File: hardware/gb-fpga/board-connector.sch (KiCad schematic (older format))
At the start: 1 part, among them J5 Conn_02x25_Counter_Clockwise

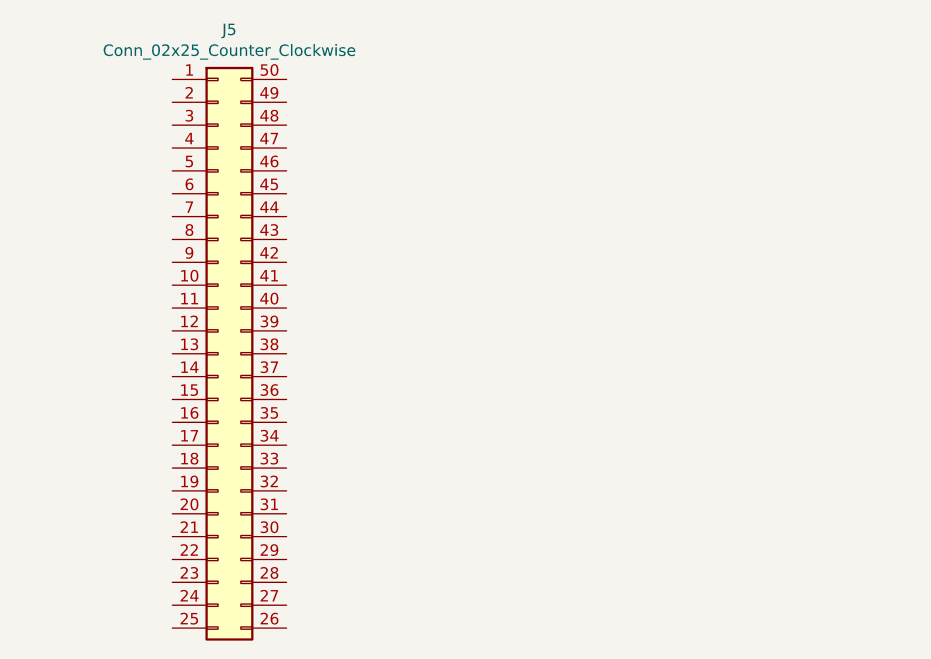
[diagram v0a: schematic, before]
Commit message: Add signals to board connector
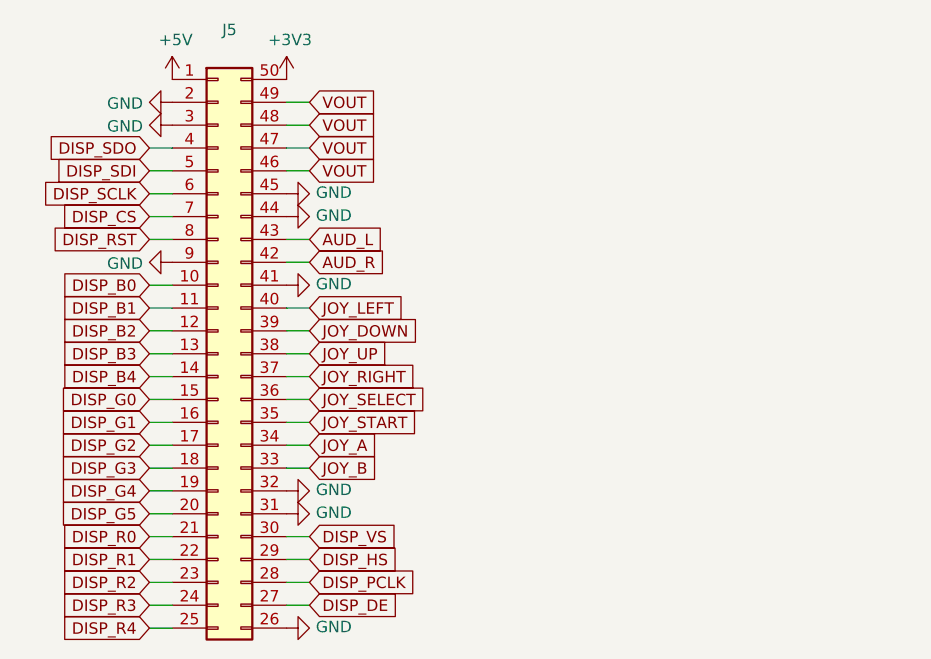
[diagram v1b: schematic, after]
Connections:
- net +5V: now reaches J5.1 (Pin_1)
- net DISP_B0: now reaches J5.10 (Pin_10)
- net DISP_B1: now reaches J5.11 (Pin_11)
- net DISP_B2: now reaches J5.12 (Pin_12)
- net DISP_B3: now reaches J5.13 (Pin_13)
- net DISP_B4: now reaches J5.14 (Pin_14)
- net DISP_G0: now reaches J5.15 (Pin_15)
- net DISP_G1: now reaches J5.16 (Pin_16)
- net DISP_G2: now reaches J5.17 (Pin_17)
- net DISP_G3: now reaches J5.18 (Pin_18)
- net DISP_G4: now reaches J5.19 (Pin_19)
- net GND: now reaches J5.2 (Pin_2)
- net GND: now also J5.26 (Pin_26), J5.3 (Pin_3), J5.31 (Pin_31), J5.32 (Pin_32), J5.41 (Pin_41), J5.44 (Pin_44), J5.45 (Pin_45), J5.9 (Pin_9)
- net DISP_G5: now reaches J5.20 (Pin_20)
- net DISP_R0: now reaches J5.21 (Pin_21)
- net DISP_R1: now reaches J5.22 (Pin_22)
- net DISP_R2: now reaches J5.23 (Pin_23)
- net DISP_R3: now reaches J5.24 (Pin_24)
- net DISP_R4: now reaches J5.25 (Pin_25)
- net DISP_DE: now reaches J5.27 (Pin_27)
- net DISP_PCLK: now reaches J5.28 (Pin_28)
- net DISP_HS: now reaches J5.29 (Pin_29)
- net DISP_VS: now reaches J5.30 (Pin_30)
- net JOY_B: now reaches J5.33 (Pin_33)
- net JOY_A: now reaches J5.34 (Pin_34)
- net JOY_START: now reaches J5.35 (Pin_35)
- net JOY_SELECT: now reaches J5.36 (Pin_36)
- net JOY_RIGHT: now reaches J5.37 (Pin_37)
- net JOY_UP: now reaches J5.38 (Pin_38)
- net JOY_DOWN: now reaches J5.39 (Pin_39)
- net DISP_SDO: now reaches J5.4 (Pin_4)
- net JOY_LEFT: now reaches J5.40 (Pin_40)
- net AUD_R: now reaches J5.42 (Pin_42)
- net AUD_L: now reaches J5.43 (Pin_43)
- net VOUT: now reaches J5.46 (Pin_46)
- net VOUT: now also J5.47 (Pin_47), J5.48 (Pin_48), J5.49 (Pin_49)
- net DISP_SDI: now reaches J5.5 (Pin_5)
- net +3V3: now reaches J5.50 (Pin_50)
- net DISP_SCLK: now reaches J5.6 (Pin_6)
- net DISP_CS: now reaches J5.7 (Pin_7)
- net DISP_RST: now reaches J5.8 (Pin_8)

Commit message: Add audio filter and volume control to schematic
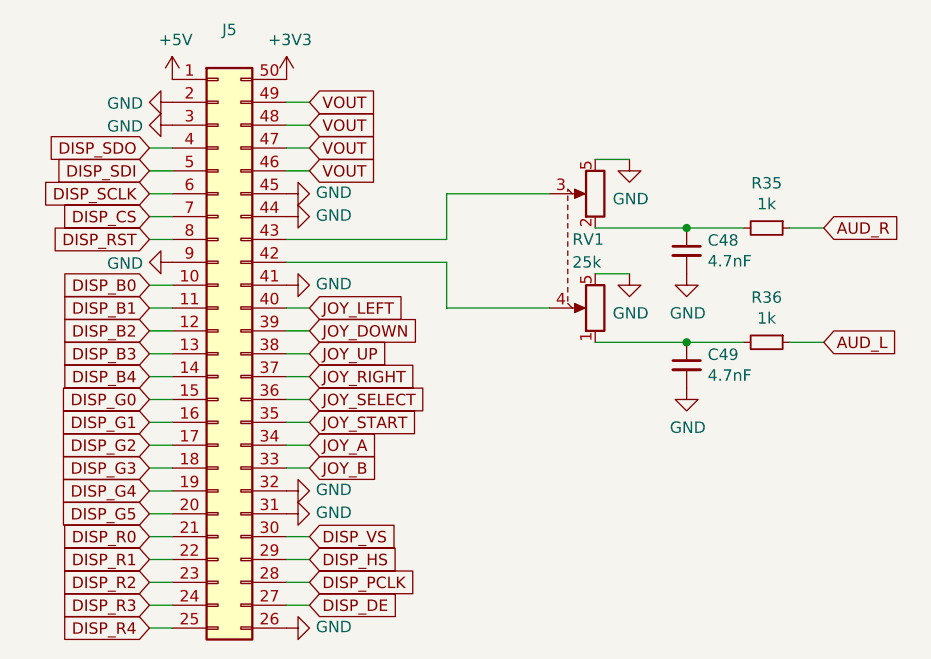
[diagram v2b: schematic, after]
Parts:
- added C48, C49: 4.7nF, Capacitor_SMD:C_0402_1005Metric, symbol Device:C_Small
- added R35, R36: 1k, Resistor_SMD:R_0402_1005Metric, symbol Device:R_Small
- added RV1: 25k, symbol gb-fpga:R_POT_Dual
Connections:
- net AUD_L: now also R36.1; no longer J5.43 (Pin_43)
- net AUD_R: now also R35.1; no longer J5.42 (Pin_42)
- net GND: now also C48.2, C49.2, RV1.5
- new net: J5.42 (Pin_42), RV1.4
- new net: J5.43 (Pin_43), RV1.3
- new net: C48.1, R35.2, RV1.2
- new net: C49.1, R36.2, RV1.1
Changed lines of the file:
@@
 	0    -1   -1   0
 $EndComp
-Text GLabel 6000 3300 2    50   Input ~ 0
+Text GLabel 8250 3150 2    50   Input ~ 0
 AUD_R
 Wire Wire Line
@@
 Text GLabel 6000 2700 2    50   Input ~ 0
 VOUT
-Wire Wire Line
-	5900 3200 6000 3200
 $Comp
 L power:GND #PWR0195
@@
 	0    1    1    0
 $EndComp
-Text GLabel 6000 3200 2    50   Input ~ 0
+Text GLabel 8250 3650 2    50   Input ~ 0
 AUD_L
-Wire Wire Line
-	6000 3300 5900 3300
 Wire Wire Line
 	6000 2800 5900 2800
@@
 	6000 2900 5900 2900
 $Comp
-L power:+3V3 #PWR?
+L power:+3V3 #PWR0196
 U 1 1 60E17B51
 P 5900 2500
-F 0 "#PWR?" H 5900 2350 50  0001 C CNN
+F 0 "#PWR0196" H 5900 2350 50  0001 C CNN
 F 1 "+3V3" H 5915 2673 50  0000 C CNN
 F 2 "" H 5900 2500 50  0001 C CNN
@@
 	1    0    0    -1
 $EndComp
+$Comp
+L Device:R_Small R35
+U 1 1 60DEF326
+P 8000 3150
+F 0 "R35" V 7804 3150 50  0000 C CNN
+F 1 "1k" V 7895 3150 50  0000 C CNN
+F 2 "Resistor_SMD:R_0402_1005Metric" H 8000 3150 50  0001 C CNN
+F 3 "~" H 8000 3150 50  0001 C CNN
+	1    8000 3150
+	0    1    1    0
+$EndComp
+$Comp
+L Device:R_Small R36
+U 1 1 60DEF85D
+P 8000 3650
+F 0 "R36" V 7804 3650 50  0000 C CNN
+F 1 "1k" V 7895 3650 50  0000 C CNN
+F 2 "Resistor_SMD:R_0402_1005Metric" H 8000 3650 50  0001 C CNN
+F 3 "~" H 8000 3650 50  0001 C CNN
+	1    8000 3650
+	0    1    1    0
+$EndComp
+$Comp
+L Device:C_Small C48
+U 1 1 60DF013C
+P 7650 3250
+F 0 "C48" H 7742 3296 50  0000 L CNN
+F 1 "4.7nF" H 7742 3205 50  0000 L CNN
+F 2 "Capacitor_SMD:C_0402_1005Metric" H 7650 3250 50  0001 C CNN
+F 3 "~" H 7650 3250 50  0001 C CNN
+	1    7650 3250
+	1    0    0    -1
+$EndComp
+$Comp
+L Device:C_Small C49
+U 1 1 60DF0823
+P 7650 3750
+F 0 "C49" H 7742 3796 50  0000 L CNN
+F 1 "4.7nF" H 7742 3705 50  0000 L CNN
+F 2 "Capacitor_SMD:C_0402_1005Metric" H 7650 3750 50  0001 C CNN
+F 3 "~" H 7650 3750 50  0001 C CNN
+	1    7650 3750
+	1    0    0    -1
+$EndComp
+Wire Wire Line
+	8250 3150 8100 3150
+Wire Wire Line
+	7900 3150 7650 3150
+Wire Wire Line
+	6600 3000 6600 3200
+Wire Wire Line
+	5900 3200 6600 3200
+Wire Wire Line
+	8250 3650 8100 3650
+Wire Wire Line
+	7900 3650 7650 3650
+Wire Wire Line
+	6600 3500 6600 3300
+Wire Wire Line
+	5900 3300 6600 3300
+$Comp
+L power:GND #PWR0197
+U 1 1 60DF887F
+P 7650 3350
+F 0 "#PWR0197" H 7650 3100 50  0001 C CNN
+F 1 "GND" H 7655 3177 50  0000 C CNN
+F 2 "" H 7650 3350 50  0001 C CNN
+F 3 "" H 7650 3350 50  0001 C CNN
+	1    7650 3350
+	1    0    0    -1
+$EndComp
+$Comp
+L power:GND #PWR0198
+U 1 1 60DF88E6
+P 7650 3850
+F 0 "#PWR0198" H 7650 3600 50  0001 C CNN
+F 1 "GND" H 7655 3677 50  0000 C CNN
+F 2 "" H 7650 3850 50  0001 C CNN
+F 3 "" H 7650 3850 50  0001 C CNN
+	1    7650 3850
+	1    0    0    -1
+$EndComp
+$Comp
+L gb-fpga:R_POT_Dual RV1
+U 1 1 60DF9C86
+P 7150 3250
+F 0 "RV1" V 7200 3250 50  0000 R CNN
+F 1 "25k" V 7100 3250 50  0000 R CNN
+F 2 "" H 7400 3175 50  0001 C CNN
+F 3 "~" H 7400 3175 50  0001 C CNN
+	1    7150 3250
+	0    -1   -1   0
+$EndComp
+Wire Wire Line
+	7650 3150 7250 3150
+Connection ~ 7650 3150
+Wire Wire Line
+	7650 3650 7250 3650
+Connection ~ 7650 3650
+Wire Wire Line
+	7050 3000 6600 3000
+Wire Wire Line
+	7050 3500 6600 3500
+$Comp
+L power:GND #PWR0199
+U 1 1 60E10420
+P 7400 2850
+F 0 "#PWR0199" H 7400 2600 50  0001 C CNN
+F 1 "GND" H 7405 2677 50  0000 C CNN
+F 2 "" H 7400 2850 50  0001 C CNN
+F 3 "" H 7400 2850 50  0001 C CNN
+	1    7400 2850
+	1    0    0    -1
+$EndComp
+$Comp
+L power:GND #PWR0200
+U 1 1 60E10808
+P 7400 3350
+F 0 "#PWR0200" H 7400 3100 50  0001 C CNN
+F 1 "GND" H 7405 3177 50  0000 C CNN
+F 2 "" H 7400 3350 50  0001 C CNN
+F 3 "" H 7400 3350 50  0001 C CNN
+	1    7400 3350
+	1    0    0    -1
+$EndComp
+Wire Wire Line
+	7250 3350 7400 3350
+Wire Wire Line
+	7250 2850 7400 2850
 $EndSCHEMATC

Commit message: Add volume control footprint
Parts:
- RV1: footprint (none) -> gb-fpga:Dual_Pot
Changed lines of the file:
@@
 F 0 "RV1" V 7200 3250 50  0000 R CNN
 F 1 "25k" V 7100 3250 50  0000 R CNN
-F 2 "" H 7400 3175 50  0001 C CNN
+F 2 "gb-fpga:Dual_Pot" H 7400 3175 50  0001 C CNN
 F 3 "~" H 7400 3175 50  0001 C CNN
 	1    7150 3250

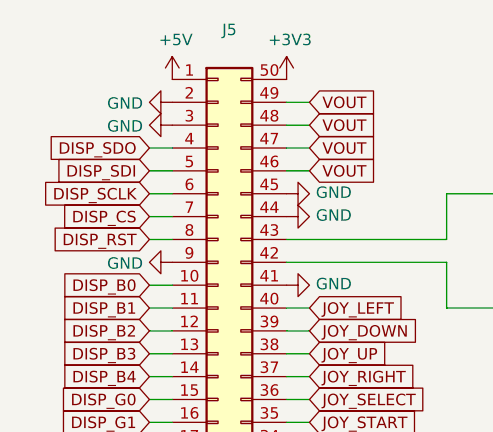
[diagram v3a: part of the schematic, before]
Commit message: Assign board connector pins to fpga
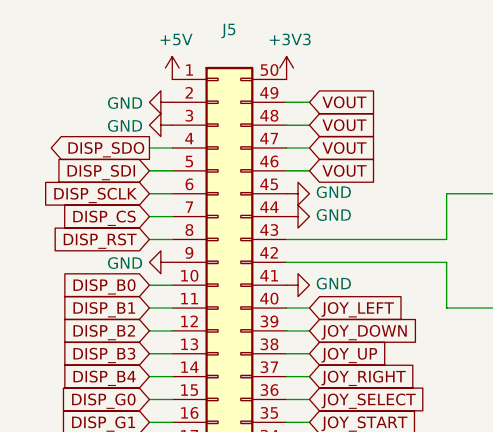
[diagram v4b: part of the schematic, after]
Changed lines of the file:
@@
 Text GLabel 5300 2900 0    50   Input ~ 0
 DISP_SDI
-Text GLabel 5300 2800 0    50   Input ~ 0
+Text GLabel 5300 2800 0    50   Output ~ 0
 DISP_SDO
 $Comp

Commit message: Update bom
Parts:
- C48, C49: Manufacturer Part Number (none) -> CL05B472KA5NNNC
- J5: Manufacturer Part Number (none) -> FH12-50S-0.5SH(55)
- R35, R36: Manufacturer Part Number (none) -> RC0402JR-071KL
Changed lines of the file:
@@
 F 2 "Connector_FFC-FPC:Hirose_FH12-50S-0.5SH_1x50-1MP_P0.50mm_Horizontal" H 5600 3700 50  0001 C CNN
 F 3 "~" H 5600 3700 50  0001 C CNN
+F 4 "FH12-50S-0.5SH(55)" H 5600 3700 50  0001 C CNN "Manufacturer Part Number"
 	1    5600 3700
 	1    0    0    -1
@@
 F 2 "Resistor_SMD:R_0402_1005Metric" H 8000 3150 50  0001 C CNN
 F 3 "~" H 8000 3150 50  0001 C CNN
+F 4 "RC0402JR-071KL" H 8000 3150 50  0001 C CNN "Manufacturer Part Number"
 	1    8000 3150
 	0    1    1    0
@@
 F 2 "Resistor_SMD:R_0402_1005Metric" H 8000 3650 50  0001 C CNN
 F 3 "~" H 8000 3650 50  0001 C CNN
+F 4 "RC0402JR-071KL" H 8000 3650 50  0001 C CNN "Manufacturer Part Number"
 	1    8000 3650
 	0    1    1    0
@@
 F 2 "Capacitor_SMD:C_0402_1005Metric" H 7650 3250 50  0001 C CNN
 F 3 "~" H 7650 3250 50  0001 C CNN
+F 4 "CL05B472KA5NNNC" H 7650 3250 50  0001 C CNN "Manufacturer Part Number"
 	1    7650 3250
 	1    0    0    -1
@@
 F 2 "Capacitor_SMD:C_0402_1005Metric" H 7650 3750 50  0001 C CNN
 F 3 "~" H 7650 3750 50  0001 C CNN
+F 4 "CL05B472KA5NNNC" H 7650 3750 50  0001 C CNN "Manufacturer Part Number"
 	1    7650 3750
 	1    0    0    -1
